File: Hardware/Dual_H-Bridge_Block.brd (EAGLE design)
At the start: 30.5 x 44.5 mm, 27 parts, among them U1 TB6612FNG, U2 EDISON_CONNECTOR_FULLMOUNTING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, U3 EDISON_CONNECTOR_FULLHEADER, U4 TXB0108

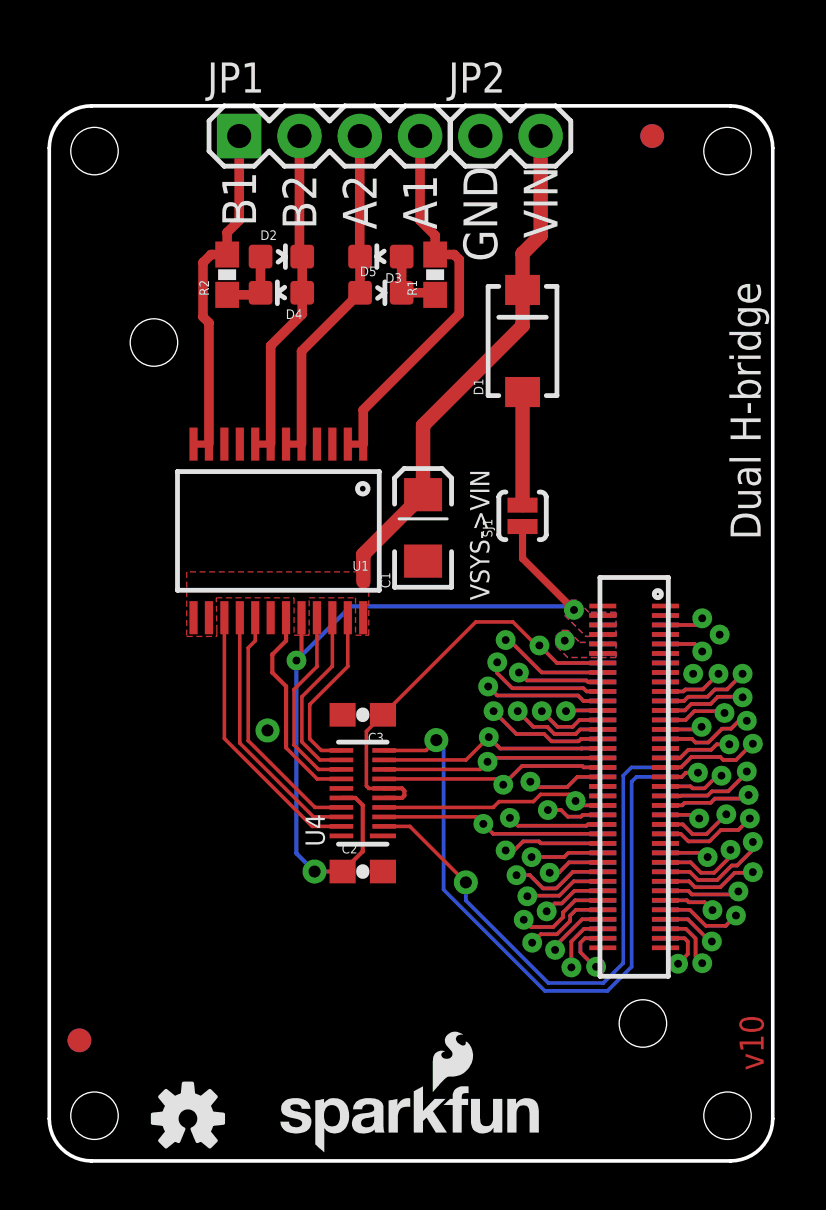
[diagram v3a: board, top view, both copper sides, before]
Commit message: Ready for reds. Change LED resistors to 680 ohm Thicken traces of drive Touch up schematic No known to-do items
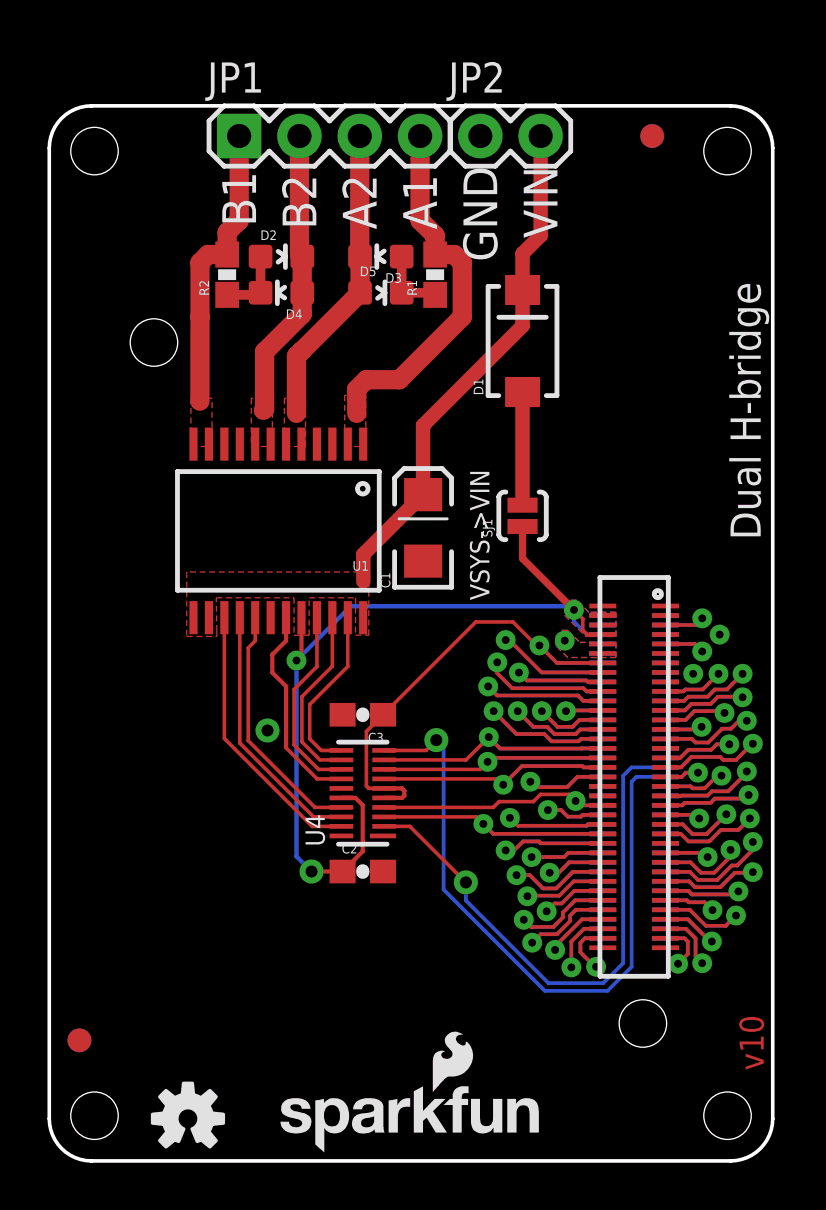
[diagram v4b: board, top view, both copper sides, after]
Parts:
- R1, R2: value 2.0k -> 680
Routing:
- net VSYS: track 33.6 -> 37.5 mm
- net B1: track 14.8 -> 12.5 mm
- net B2: track 14.2 -> 12.3 mm
- net A2: track 14.7 -> 12.8 mm
- net A1: track 16.5 -> 15.5 mm
- added copper zone on layer 1, net A1
- added copper zone on layer 1, net A2
- added copper zone on layer 1, net B1
- added copper zone on layer 1, net B2
